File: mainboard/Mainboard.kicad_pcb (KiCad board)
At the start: 4 copper layers, 106 x 80 mm, 142 parts, among them IC1001 TXB0104RUT, IC1002 PCA9306JK, IC1003 TXB0104RUT, IC1101 PCAL6416AHF, IC1102 TMP117xxYBG, IC1103 PCA9306JK, IC1104 PCA9633DP1,118, IC1105 RV-8263-C8, IC1201 TXB0102DCU, IC1202 PCA9306JK, IC701 USBLC6-2P6, IC702 BQ21040DBV, IC703 MAX17048, IC801 TPS62823DLC, IC802 LP5907MFX-2.8, IC803 LP5907MFX-1.5, IC804 LP5907MFX-3.0, IC805 LP5907MFX-2.8, IC806 LP5907MFX-1.2, M901 ESP32-S3-WROOM-1, Q1101 DMN2053UQ, Q1102 DMN2053UQ, Q701 Si2333CDS, SW701 On / Off, SW901 Reset, X1001 LEPTON, X1201 Camera, X1301 Micro SD-Card, X1401 Displayboard, X701 USB, X702 Battery, X901 Prog, Y1001 25 MHz, Y1201 25 MHz

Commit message: Update outputs (release)
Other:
- board text added: "0.035mm (1.00oz)"
- board text added: "0.196mm"
- board text added: "1.03mm"
- board text added: "Inner1 (GND)"
- board text added: "Inner2"
- board text added: "Plane"
- board text added: "Prepreg"
- board text added: "Total thickness: 1.582mm"
- board text removed: "0.035mm (1oz)"
- board text removed: "1.51mm"
- board text removed: "Total thickness: 1.6mm"

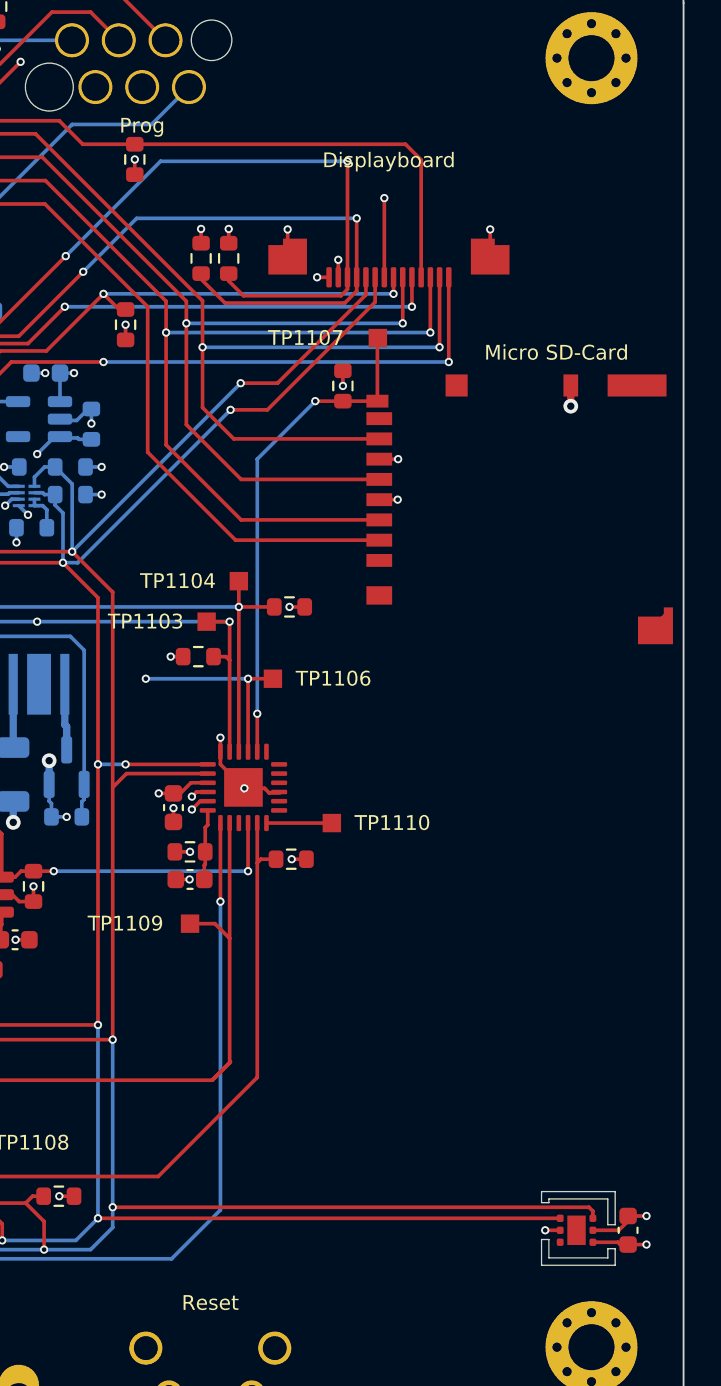
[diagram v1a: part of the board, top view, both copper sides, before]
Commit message: Task: Issue #7
- Increase the width of the cutout for the temperature sensor
- Add missing component informations
- Fix wrong component informations

Closes: #7

Signed-off-by: Daniel Kampert <DanielKampert@kampis-elektroecke.de>
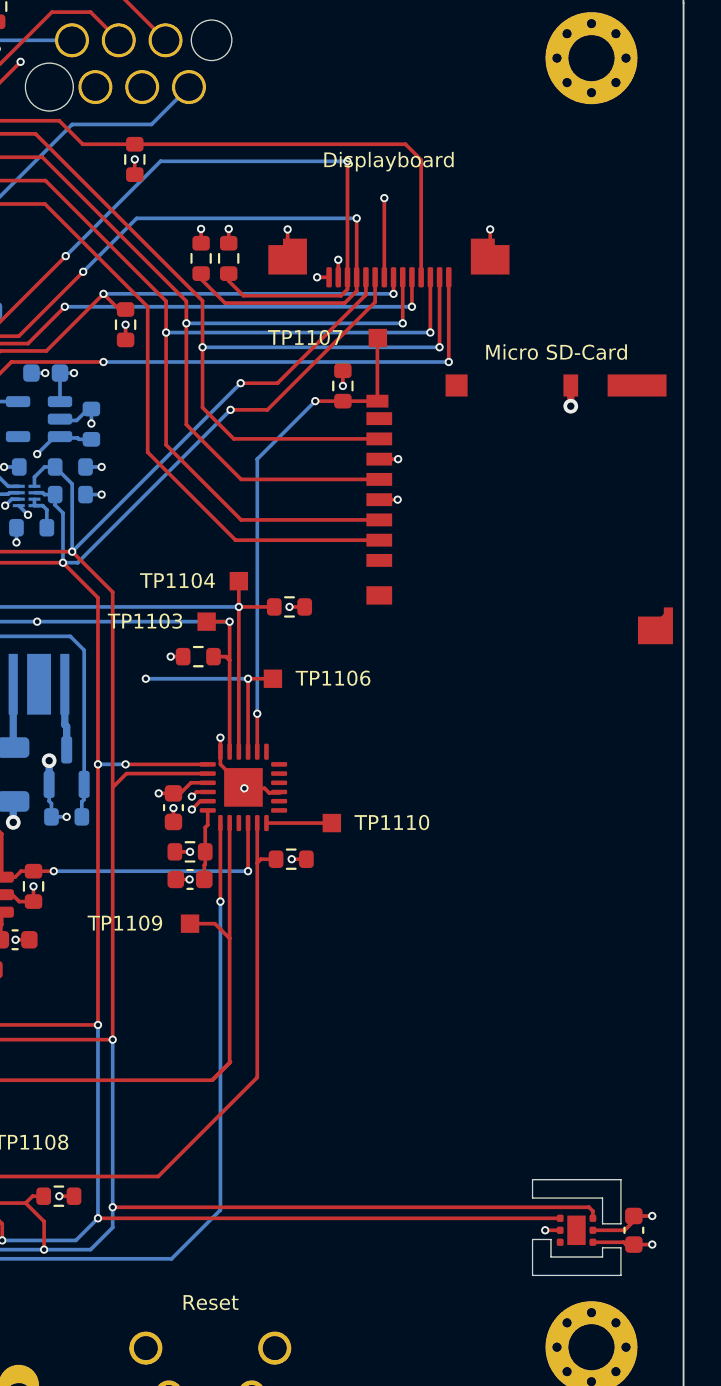
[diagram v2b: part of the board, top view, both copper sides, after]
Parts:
- moved C1103 0.31 mm to (263.3, 186.7)
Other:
- outline, holes or cut-outs redrawn
- board text added: "0.035mm (1oz)"
- board text added: "1.51mm"
- board text added: "Total thickness: 1.6mm"
- board text removed: "0.035mm (1.00oz)"
- board text removed: "0.196mm"
- board text removed: "1.03mm"
- board text removed: "Inner1 (GND)"
- board text removed: "Inner2"
- board text removed: "Plane"
- board text removed: "Prepreg"
- board text removed: "Total thickness: 1.582mm"

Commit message: Bug: Issue #8
- Drill drawing is missing

Closes: #8

Signed-off-by: Daniel Kampert <DanielKampert@kampis-elektroecke.de>
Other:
- board text added: "Drill Table"
